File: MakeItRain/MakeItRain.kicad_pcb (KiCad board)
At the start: 4 copper layers, 151.1 x 71.1 mm, 84 parts, among them IC1 MCP23008T-E_SS, IC3 OPA2340PA, IC4 LTV-846S, J1 Conn_02x14_Odd_Even, J2 Conn_02x19_Odd_Even, J3 Conn_01x19, J4 Conn_01x01, J5 Conn_01x03, P1 Screw_Terminal_01x02, Q1 2N7000, Q10 2N7000, Q11 2N7000, Q12 IRF9Z34NPBF, Q13 IRF9Z34NPBF, Q2 2N7000, Q3 IRF9Z34NPBF, Q4 2N7000, Q5 2N7000, Q6 IRF9Z34NPBF, Q7 2N7000, Q8 2N7000, Q9 IRF9Z34NPBF, U2 178.6165.0001

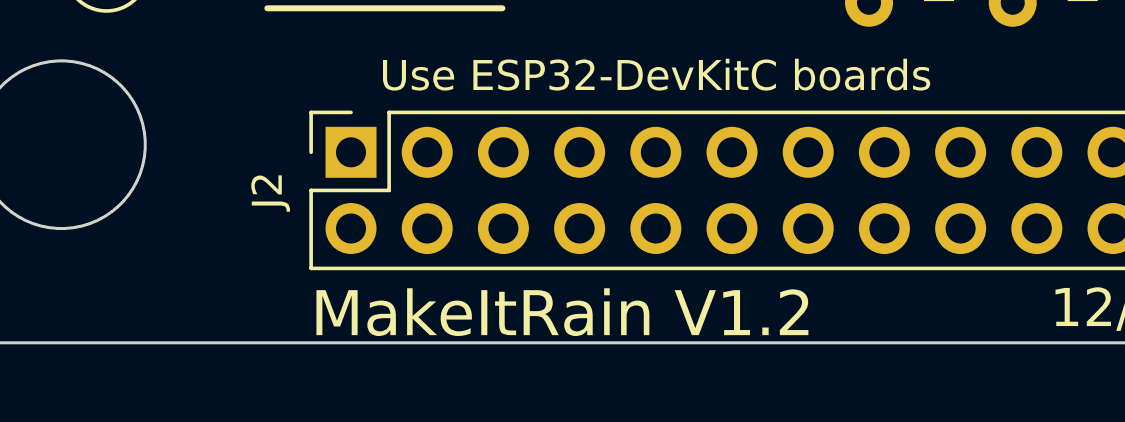
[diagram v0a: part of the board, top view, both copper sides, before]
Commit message: fixed the 3d shapes for various parts
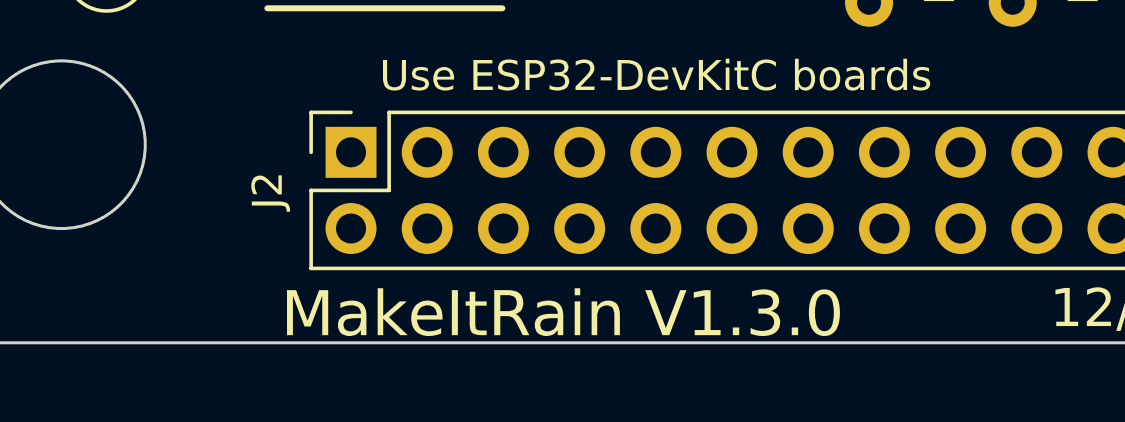
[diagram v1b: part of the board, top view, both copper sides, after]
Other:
- board text added: "MakeItRain V1.3.0"
- board text removed: "MakeItRain V1.2"

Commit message: updating some routes, updating the already done daughterboard and updating the blank layout for both.
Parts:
- moved D8 10.2 mm to (185.6, 76.2), turned to -90 degrees
- moved R35 3.01 mm to (190.3, 80.1), turned to -90 degrees
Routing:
- net +3V3: track 35.4 -> 10.0 mm
- net GND: track 223.2 -> 236.4 mm
- net Net-(J2-Pad37): track 0.00 -> 2.54 mm
- net EN: track 0.00 -> 2.54 mm
- net D39: track 0.00 -> 2.54 mm
- net D36: track 0.00 -> 2.54 mm
- net D35: track 0.00 -> 2.54 mm
- net D34: track 0.00 -> 2.54 mm
- net D33: track 0.00 -> 2.54 mm
- net D32: track 0.00 -> 2.54 mm
- net D27: track 0.00 -> 2.54 mm
- net D26: track 0.00 -> 2.54 mm
- net D25: track 0.00 -> 2.54 mm
- net D14: track 0.00 -> 2.54 mm
- net D12: track 0.00 -> 2.54 mm

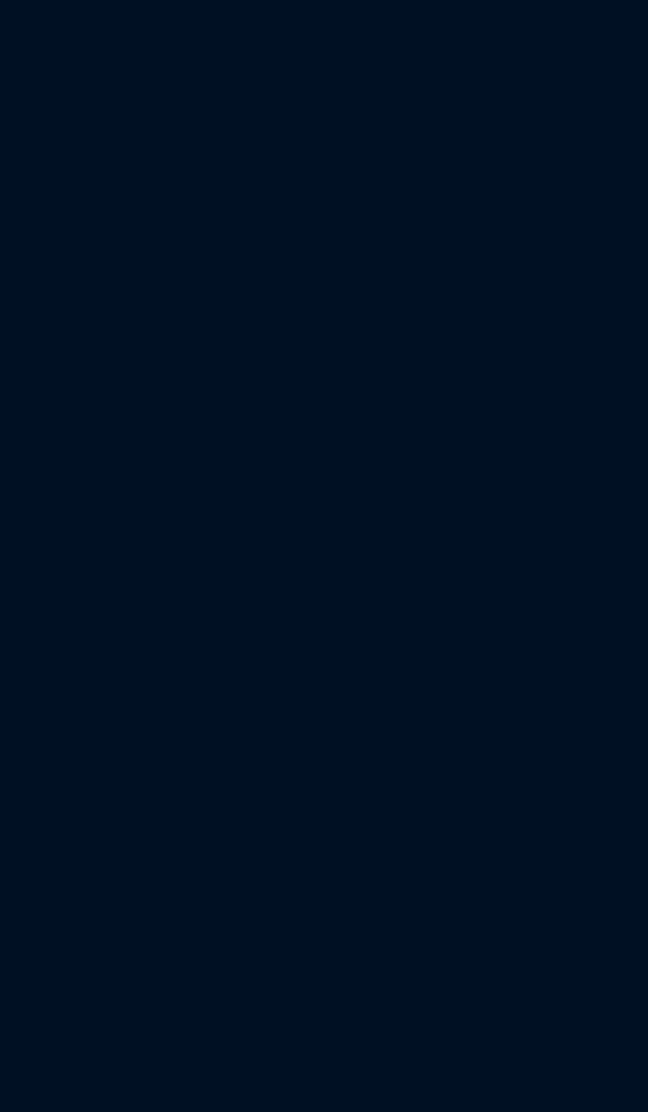
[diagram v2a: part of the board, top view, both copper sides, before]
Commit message: Moving into the prototyping testing this deisgn completely phase.
changes
* remapping some pins cause i forgot that ADC2 can not be used while using wifi.
* adding the TH version of the MCP230008 as i don't know the availability of these chips can populate one or the other
* removed zones 5-8 in the code since i hhaven't figured out the daughter board yet. Code not included can be buggy
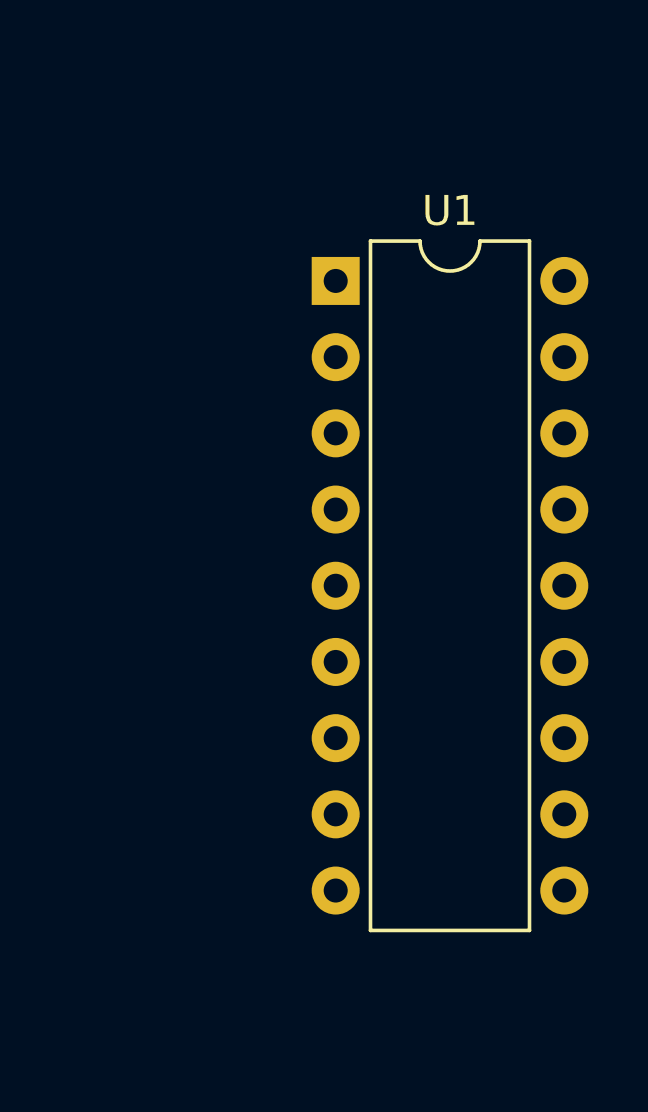
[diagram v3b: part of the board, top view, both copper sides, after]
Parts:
- added U1: MCP23008-xP, Package_DIP:DIP-18_W7.62mm, F.Cu at (209.6, 89.7)
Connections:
- IC3 pad 1: D25 -> D33
- IC3 pad 2: D25 -> D33
- R25 pad 1: D25 -> D33
- R3 pad 1: D33 -> D25
- S1 pad 4: D33 -> D25

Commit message: moving some things around.
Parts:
- moved RV1 53.4 mm to (199.5, 123.7)
- moved J4 53.4 mm to (204.8, 118.4)
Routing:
- net GND: track 236.4 -> 227.4 mm
- net AuxVoltage: track 8.72 -> 0.00 mm

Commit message: placing parts
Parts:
- moved U1 93.6 mm to (116.3, 96.9)
- moved J4 54.3 mm to (155.6, 95.3)
- moved RV1 54.3 mm to (150.3, 100.6)
- moved R36 7.10 mm to (110.5, 105.9)
- moved IC1 6.72 mm to (109.9, 113.0)
- moved R38 4.61 mm to (102.0, 107.1)
- moved R37 4.61 mm to (102.0, 102.4)
- moved R3 4.45 mm to (102.8, 112.2)
- moved R30 4.39 mm to (79.0, 112.1)
- moved R32 4.39 mm to (88.6, 112.1)
- moved R33 4.39 mm to (93.4, 112.1)
- moved R4 4.39 mm to (98.1, 112.2)
- moved R31 4.39 mm to (83.8, 112.1)
- moved Q1 3.19 mm to (79.1, 103.7)
- moved Q4 3.19 mm to (84.7, 103.7)
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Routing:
- net GND: track 227.4 -> 193.6 mm

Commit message: partial routing need to finish out the remainder.
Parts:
- IC1: moved to B.Cu
- turned IC1 to 180 degrees
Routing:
- net +3V3: track 10.0 -> 213.7 mm, vias 0 -> 1
- net GND: track 193.6 -> 347.7 mm, vias 3 -> 6
- net D23: track 0.00 -> 138.9 mm, vias 0 -> 1
- net D22: track 0.00 -> 136.2 mm, vias 0 -> 1
- net TX: track 0.00 -> 131.8 mm
- net D21: track 0.00 -> 124.2 mm, vias 0 -> 4
- net Net-(D8-Pad2): track 0.00 -> 111.6 mm, vias 0 -> 1
- net D19: track 0.00 -> 105.8 mm, vias 0 -> 1
- net Net-(IC3-Pad5): track 0.00 -> 94.2 mm
- net RX: track 0.00 -> 86.2 mm, vias 0 -> 1
- net Z8: track 0.00 -> 85.9 mm, vias 0 -> 3
- net Z3: track 0.00 -> 83.2 mm, vias 0 -> 2
- net D35: track 2.54 -> 80.2 mm, vias 0 -> 2
- net D18: track 0.00 -> 75.8 mm, vias 0 -> 1
- net D16: track 0.00 -> 74.5 mm
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
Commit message: almost finished some routes
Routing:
- net /InputIsolation/2in: track 0.00 -> 60.8 mm
- net D36: track 27.9 -> 77.3 mm
- net D39: track 26.6 -> 68.4 mm
- net GND: track 347.7 -> 371.7 mm, vias 6 -> 5
- net Z1: track 73.5 -> 96.3 mm
- net Z2: track 40.0 -> 59.3 mm
- net Net-(IC1-Pad6): track 9.97 -> 19.9 mm
- net Z6: track 45.4 -> 50.7 mm, vias 0 -> 1
- net Z5: track 41.5 -> 44.9 mm, vias 0 -> 1
- net Z4: track 70.5 -> 73.8 mm, vias 1 -> 2
- net Z8: track 85.9 -> 86.2 mm, vias 3 -> 2

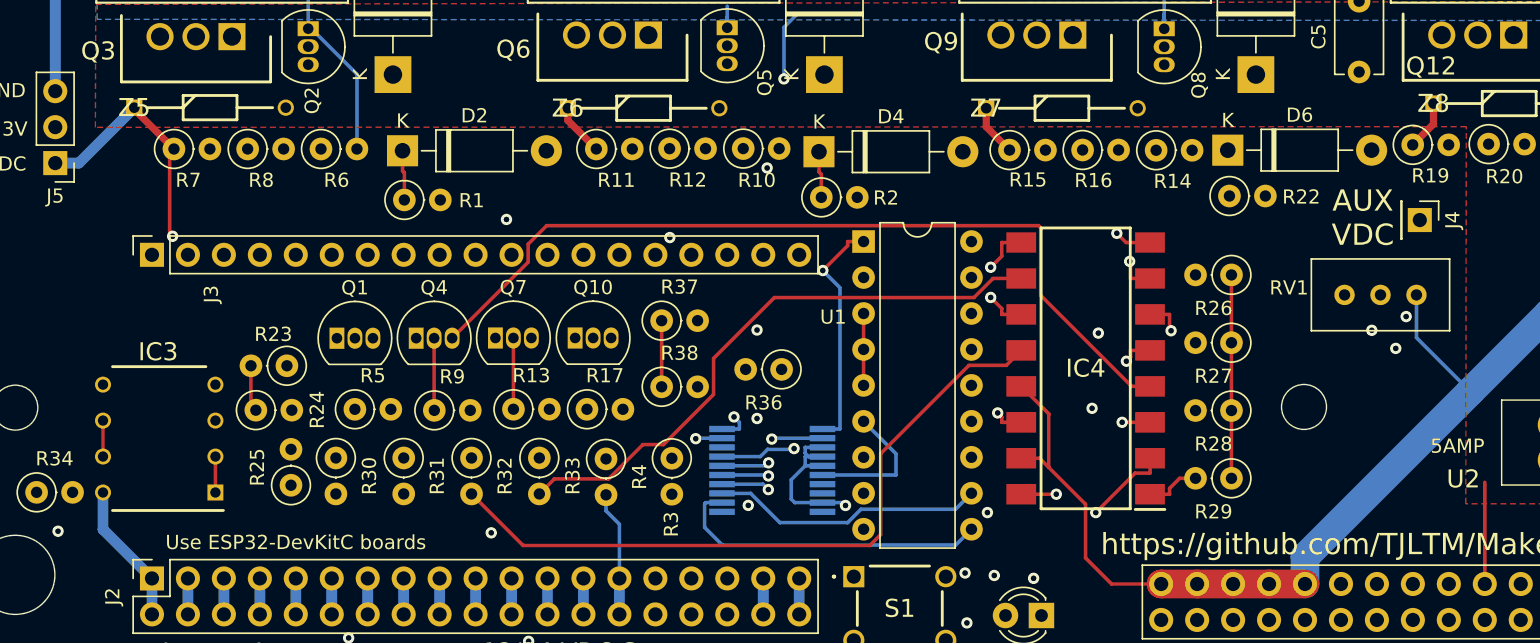
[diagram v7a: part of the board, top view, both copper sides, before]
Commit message: Finished routing, DRC'ed and new Fab Files. Need one more once over to check before sending off to FAB
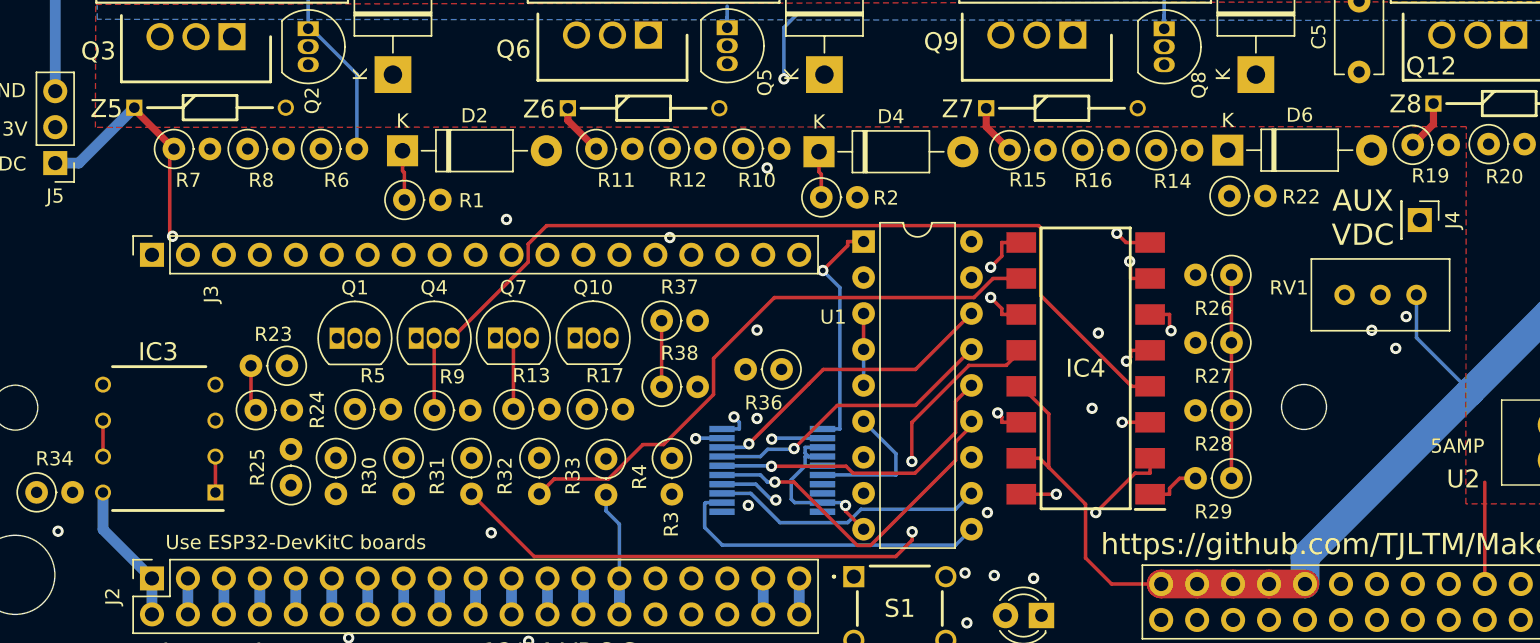
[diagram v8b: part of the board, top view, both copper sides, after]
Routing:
- net Z7: track 49.2 -> 70.7 mm, vias 0 -> 1
- net Z4: track 73.8 -> 94.7 mm
- net Z5: track 44.9 -> 63.2 mm
- net Z6: track 50.7 -> 66.1 mm
- net D36: track 77.3 -> 79.5 mm, vias 0 -> 2
- net Z3: track 83.5 -> 84.2 mm
